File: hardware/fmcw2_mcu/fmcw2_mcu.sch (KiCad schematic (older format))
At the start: 123 parts, among them CON1 BARREL_JACK, P1 CONN_15X2, P2 CONN_1, P3 CONN_1, P4 CONN_1, P5 CONN_1, P6 CONN_5, P7 CONN_6, Q1 RE1C002UN, Q2 RE1C002UN, SW1 DFU_PUSH, SW2 DFU_PUSH, U1 MAX1426, U16 USB-MICRO, U2 LT1817, U3 W25Q32FV, U4 LPC4320_BGA, U5 AOZ1281, U6 AOZ1281, U7 LP2985, U8 MCP4022-202, U9 FDC6329L, X1 12MHz

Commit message: Rescue schematic symbols to a new library
Schematic used old symbols and without cached library files
uses instead the new symbols that have different pin pitch.
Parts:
- C1, C10, C11, C12, C13, C14, C15, C16, C17, C18, C19, C2, C20, C21, C22, C23, C24, C25, C26, C27, C28, C29, C3, C30, C31, C32, C33, C34, C35, C36, C37, C38, C39, C4, C40, C41, C42, C43, C44, C45, C46, C47, C48, C49, C5, C50, C51, C52, C6, C7, C8, C9: symbol C -> C-RESCUE-fmcw2_mcu
- D1, D2: symbol LED -> LED-RESCUE-fmcw2_mcu
- R1, R10, R11, R12, R13, R14, R15, R16, R17, R18, R19, R2, R20, R21, R22, R23, R24, R25, R26, R27, R28, R29, R3, R30, R31, R32, R33, R34, R35, R36, R37, R38, R39, R4, R40, R41, R42, R5, R6, R7, R8, R9: symbol R -> R-RESCUE-fmcw2_mcu

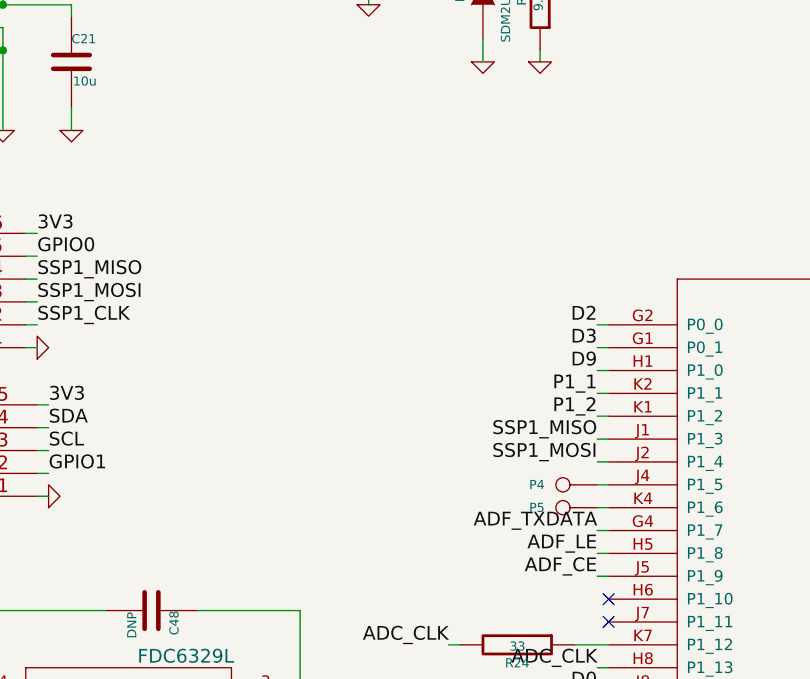
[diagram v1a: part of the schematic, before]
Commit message: Add jump wire transistor
Scretches the ramp complete pulse from ADF4158.
Internal pull-up resistor of the microcontroller pin is used
to pull-up the transistor drain.
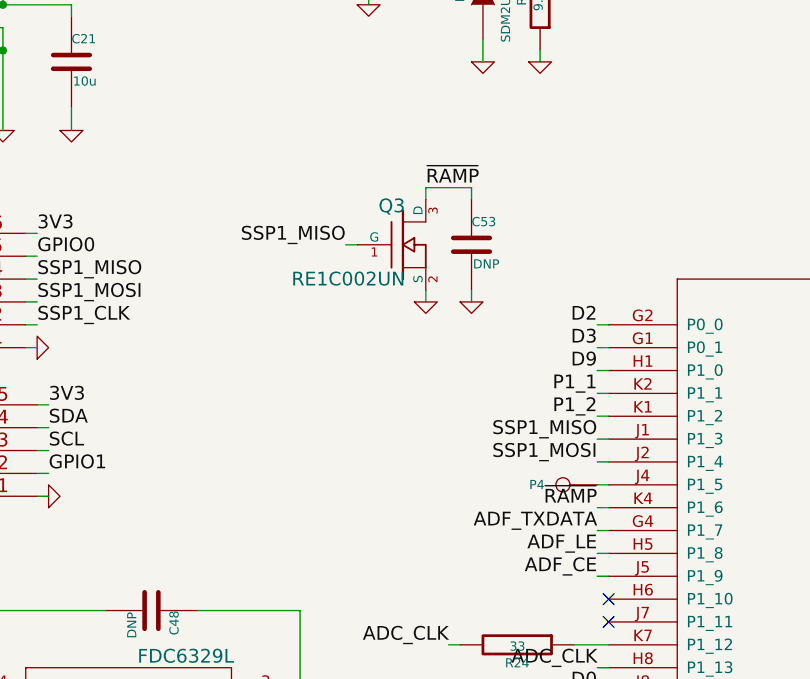
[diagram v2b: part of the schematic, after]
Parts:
- removed P5: CONN_1, fmcw2:TP_1.00, symbol CONN_1
- added C53: DNP, fmcw2:C_0402b, symbol C-RESCUE-fmcw2_mcu
- added Q3: RE1C002UN, fmcw2:SOT-416, symbol MOS_N_GSD
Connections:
- net GND: now also C53.2, Q3.2 (S)
- net SSP1_MISO: now also Q3.1 (G)
- net ~RAMP: now reaches U4.K4 (P1_6)
- net ~RAMP: now also C53.1, Q3.3 (D)

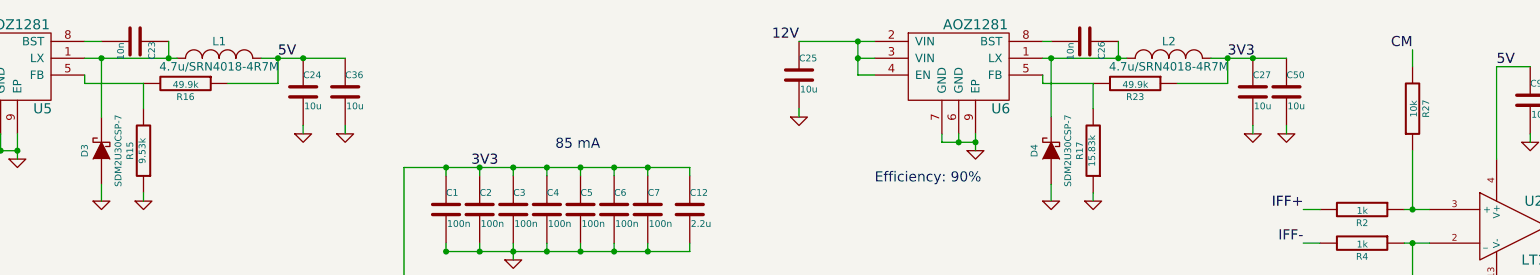
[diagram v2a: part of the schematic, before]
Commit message: Change inductors to better shielded ones
Previous inductors weren't too well shielded and radiated a lot.
Footprint is unchanged.

R27 is also changed to 1k from 10k to increase PSRR.
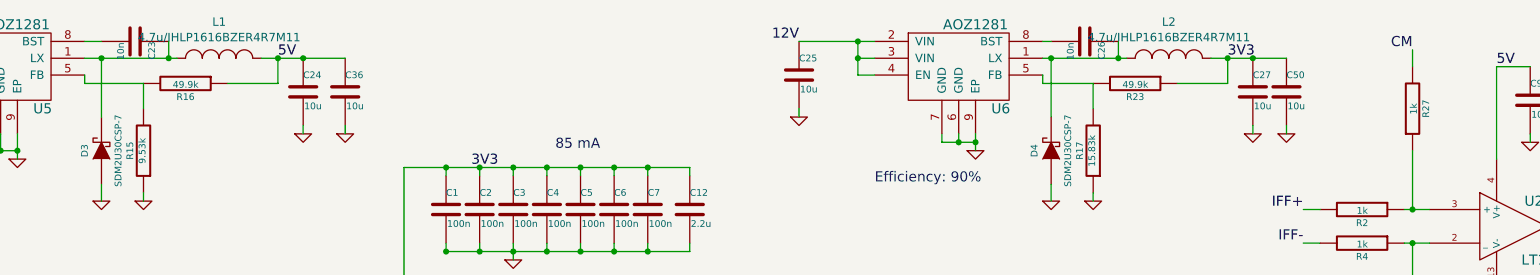
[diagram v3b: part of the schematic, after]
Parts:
- L1, L2: value 4.7u/SRN4018-4R7M -> 4.7u/IHLP1616BZER4R7M11
- R27: value 10k -> 1k
